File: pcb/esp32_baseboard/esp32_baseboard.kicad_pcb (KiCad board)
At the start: 2 copper layers, 190 x 100 mm, 50 parts, among them J1 Screw_12V_IN, J10 HOME HOME2, J12 HOME HOME3, J14 BUP-30S, J15 BUZZER 5V, J16 AOD4184 12V, J17 MSP3520 LCD, J18 EC11 ENC, J23 MSP3520 TP, J24 595_CTRL, J25 595_Q, J8 HOME HOME1, U1 ESP32-S3 DevKitC, U2 MP1584 5V, U3 TMC2209, U41 PC817, U42 PC817, U43 PC817, U44 PC817, U5 ULN2003 A1, U6 ULN2003 A2, U7 ULN2003 A3

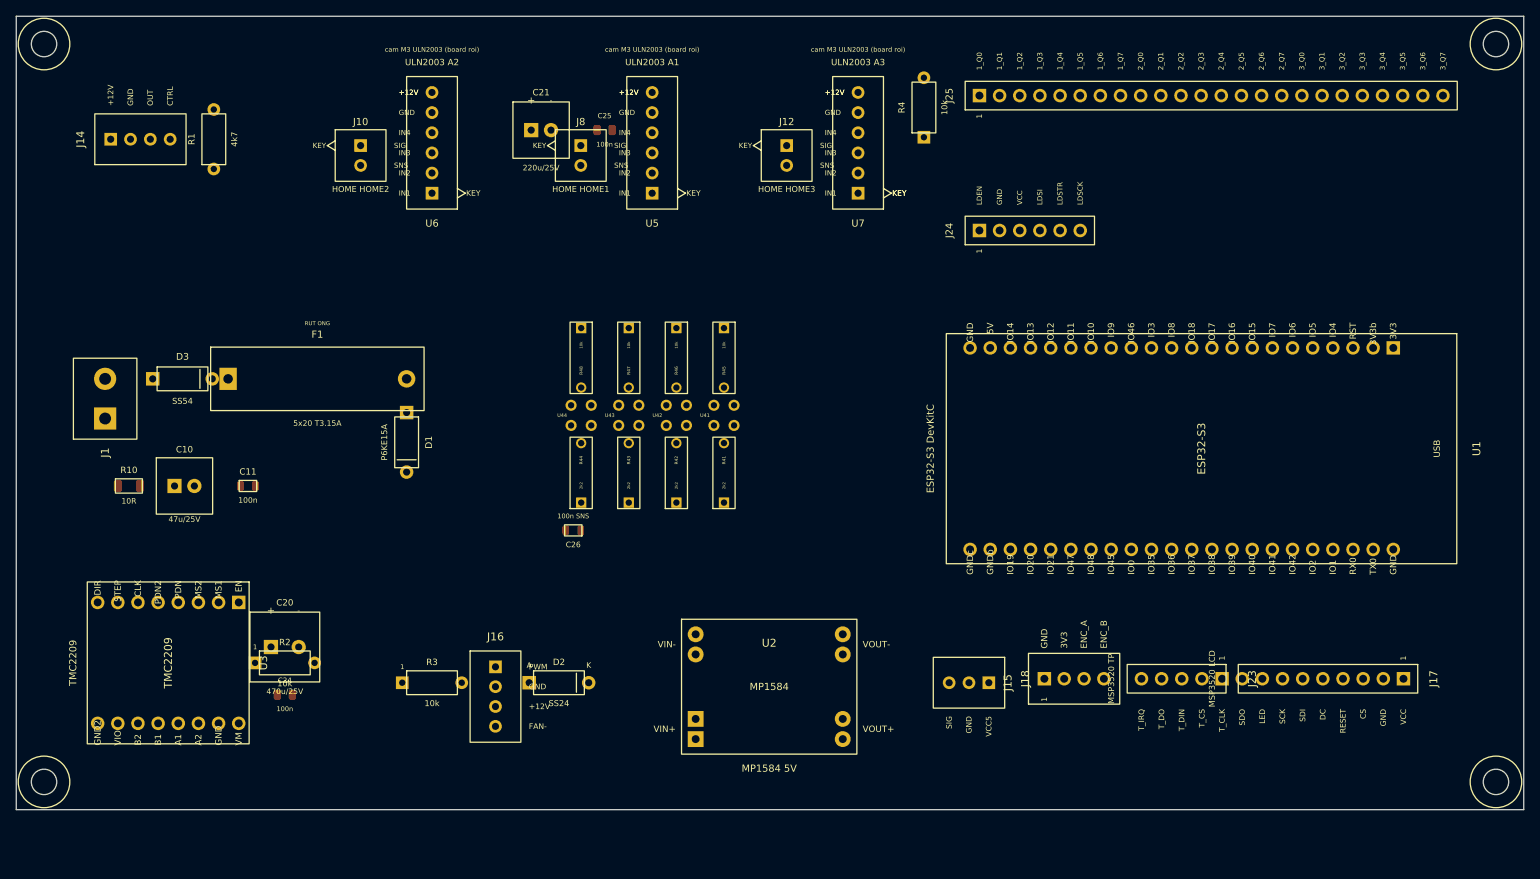
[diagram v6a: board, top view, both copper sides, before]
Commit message: update BOM và PCB với danh sách linh kiện mới loại bỏ màn hình cảm ứng và động cơ điều chỉnh độ rộng vách thay bằng led 7 thanh và bàn phím dán
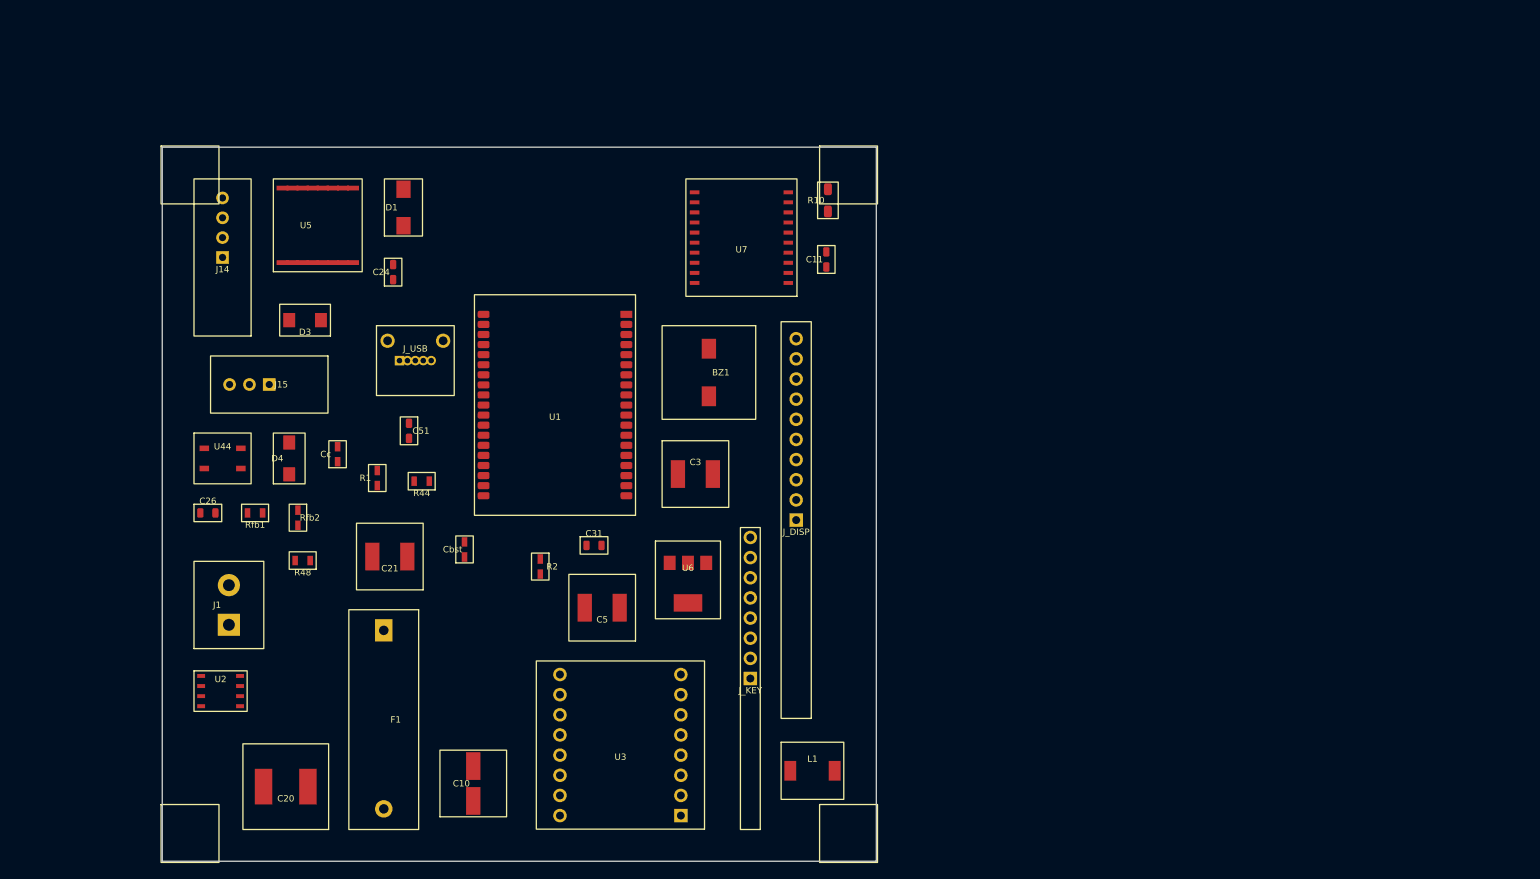
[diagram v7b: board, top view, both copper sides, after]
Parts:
- removed C25: 100n, ESP32_Carrier:C_0805_100n
- removed D2: SS24, ESP32_Carrier:Diode_TVS_DO41
- removed J10: HOME HOME2, ESP32_Carrier:JST_XH_02_Socket
- removed J12: HOME HOME3, ESP32_Carrier:JST_XH_02_Socket
- removed J16: AOD4184 12V, ESP32_Carrier:JST_XH_04_Socket
- removed J17: MSP3520 LCD, ESP32_Carrier:PinHeader_1x09_TFT_LCD
- removed J18: EC11 ENC, ESP32_Carrier:JST_XH_04_Socket
- removed J23: MSP3520 TP, ESP32_Carrier:PinHeader_1x05_TFT_TP
- removed J24: 595_CTRL, ESP32_Carrier:PinHeader_1x06_595CTRL
- removed J25: 595_Q, ESP32_Carrier:PinHeader_1x24_595Q
- removed J8: HOME HOME1, ESP32_Carrier:JST_XH_02_Socket
- removed R3, R4, R45, R46, R47: 10k, ESP32_Carrier:R_Axial_4k7_BUP
- removed R41, R42, R43: 2k2, ESP32_Carrier:R_Axial_4k7_BUP
- removed U41, U42, U43: PC817, ESP32_Carrier:PC817_DIP4
- added BZ1: BUZZ, ESP32_Carrier:Buzzer_SMD_5V, F.Cu at (118.9, 78.4)
- added C3: 47u/10V, ESP32_Carrier:CP_SMD_D6.3x5.8, F.Cu at (117.2, 91.2)
- added C31: 100n, ESP32_Carrier:C_0805_100n, F.Cu at (104.4, 100.2)
- added C5: 100u/16V, ESP32_Carrier:CP_SMD_D6.3x5.8, F.Cu at (105.4, 108.0)
- added C51: 100n, ESP32_Carrier:C_0805_100n, F.Cu at (81.1, 85.8)
- added Cbst: 10n, ESP32_Carrier:C_0805, F.Cu at (88.1, 100.7)
- added Cc: 3n3, ESP32_Carrier:C_0805, F.Cu at (72.1, 88.7)
- added D4: SS34, ESP32_Carrier:Diode_SMA, F.Cu at (66.0, 89.2)
- added J_DISP: 7SEG_EXT, ESP32_Carrier:PinHeader_1x10_7SEG, F.Cu at (129.9, 97.0)
- added J_KEY: KEYPAD_EXT, ESP32_Carrier:PinHeader_1x08_Keypad, F.Cu at (124.1, 117.0)
- added J_USB: USB, ESP32_Carrier:USB_MicroB, F.Cu at (81.9, 76.9)
- added L1: 10uH, ESP32_Carrier:L_SMD_6x6, F.Cu at (131.9, 128.6)
- added Rfb1: 52k3, ESP32_Carrier:R_0805_4k7, F.Cu at (61.7, 96.1)
- added Rfb2: 10k, ESP32_Carrier:R_0805_10k, F.Cu at (67.1, 96.7)
- C10: value 47u/25V -> 47u/50V; footprint ESP32_Carrier:CP_Radial_D6_47u_25V -> ESP32_Carrier:CP_SMD_D6.3x5.8
- C20: value 470u/25V -> 470u/50V; footprint ESP32_Carrier:CP_Radial_D8_470u_25V -> ESP32_Carrier:CP_SMD_D8x10
- C21: value 220u/25V -> 220u/50V; footprint ESP32_Carrier:CP_Radial_D6_100u_25V -> ESP32_Carrier:CP_SMD_D6.3x5.8
- C26: value 100n SNS -> 100n
- D1: value P6KE15A -> SMBJ26A; footprint ESP32_Carrier:Diode_TVS_DO41 -> ESP32_Carrier:Diode_SMB_TVS
- D3: footprint ESP32_Carrier:Diode_TVS_DO41 -> ESP32_Carrier:Diode_SMA
- F1: value 5x20 T3.15A -> T2.5A
- J1: value Screw_12V_IN -> 24V_IN
- J14: value BUP-30S -> BUP_U
- J15: value BUZZER 5V -> FIBER
- R1: footprint ESP32_Carrier:R_Axial_4k7_BUP -> ESP32_Carrier:R_0805_4k7
- R2, R48: footprint ESP32_Carrier:R_Axial_4k7_BUP -> ESP32_Carrier:R_0805_10k
- R44: footprint ESP32_Carrier:R_Axial_4k7_BUP -> ESP32_Carrier:R_0805_2k2
- U1: value ESP32-S3 DevKitC -> WROOM-32; footprint ESP32_Carrier:ESP32_S3_DevKitC_44Pin_Socket -> ESP32_Carrier:ESP32_WROOM_32
- U2: value MP1584 5V -> MP1584EN; footprint ESP32_Carrier:MP1584_5V3A -> ESP32_Carrier:MP1584EN_SOT23-8
- U3: value TMC2209 -> TMC_SOCK
- U44: footprint ESP32_Carrier:PC817_DIP4 -> ESP32_Carrier:PC817_SOP4
- U5: value ULN2003 A1 -> CH340C; footprint ESP32_Carrier:ULN2003_Module -> ESP32_Carrier:CH340C
- U6: value ULN2003 A2 -> AMS1117-3.3; footprint ESP32_Carrier:ULN2003_Module -> ESP32_Carrier:AMS1117_SOT223
- U7: value ULN2003 A3 -> TM1637; footprint ESP32_Carrier:ULN2003_Module -> ESP32_Carrier:TM1637_SOP20
- moved U1 105.9 mm to (99.5, 82.5), turned to 180 degrees
- moved J15 98.2 mm to (63.5, 79.9)
- moved R10 95.2 mm to (133.9, 56.7), turned to 90 degrees
- moved H2 83.3 mm to (136.5, 53.5)
- moved H4 81.9 mm to (136.5, 136.5)
- moved C11 78.3 mm to (133.7, 64.2), turned to 90 degrees
- moved U2 69.2 mm to (57.4, 118.6)
- moved U6 58.5 mm to (116.3, 104.5), turned to 0 degrees
- moved U3 57.9 mm to (107.7, 125.4), turned to 180 degrees
- moved C21 57.0 mm to (78.7, 101.6), turned to 180 degrees
- moved C24 55.0 mm to (79.1, 65.8), turned to 90 degrees
- moved C10 52.3 mm to (89.2, 130.2), turned to 90 degrees
- moved R1 47.4 mm to (77.1, 91.7)
- moved C26 46.1 mm to (55.8, 96.1), turned to 0 degrees
- moved U44 45.5 mm to (57.6, 89.2), turned to 0 degrees
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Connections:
- net +12V_PRE renamed +24V_PRE
- net +12V_RAW renamed +24V_RAW
- net MotA1 renamed /MotA1
- net MotA2 renamed /MotA2
- net MotB1 renamed /MotB1
- net MotB2 renamed /MotB2
- C10 pad 1: +12V_SNS -> +24V_SNS
- C11 pad 1: +12V_SNS -> +24V_SNS
- C20 pad 1: +12V -> +24V
- C21 pad 1: +12V -> +24V
- C24 pad 1: +12V -> +24V
- C26 pad 1: +12V_SNS -> +24V_SNS
- D1 pad 2: +12V -> +24V
- F1 pad 2: +12V -> +24V
- J14 pad 1: +12V_SNS -> +24V_SNS
- J14 pad 3: OPTO_IN4 -> /OPTO_IN_BUP
- J15 pad 1: +5V -> +24V_SNS
- J15 pad 3: BUZZER -> /OPTO_IN_BUP
- R1 pad 1: +12V_SNS -> +24V_SNS
- R1 pad 2: OPTO_IN4 -> /OPTO_IN_BUP
- R10 pad 1: +12V -> +24V
- R10 pad 2: +12V_SNS -> +24V_SNS
- R2 pad 1: EN_TMC -> +3V3
- R2 pad 2: +3V3 -> /EN_TMC
- R44 pad 1: OPTO_IN4 -> +24V_SNS
- R44 pad 2: OPTO_A4 -> /OPTO_IN_BUP
- R48 pad 2: OPTO_OUT4 -> /BUP
- U1 pad 1: +3V3 -> GND
- U1 pad 10: DIR -> /BUZZER
- U1 pad 11: EN_TMC -> /KEY_C0
- U1 pad 12: unconnected-(U1-IO8-Pad12) -> /KEY_R3
- U1 pad 13: BLOWER -> /KEY_R2
- U1 pad 14: TFT_RST -> /KEY_R1
- U1 pad 15: BUZZER -> GND
- U1 pad 16: SER -> /KEY_R0
- U1 pad 17: SRCLK -> unconnected-(U1-P17-Pad17)
- U1 pad 18: RCLK -> unconnected-(U1-P18-Pad18)
- U1 pad 19: OE_595 -> unconnected-(U1-P19-Pad19)
- U1 pad 20: unconnected-(U1-IO14-Pad20) -> GND
- U1 pad 21: +5V -> unconnected-(U1-P21-Pad21)
- U1 pad 22: GND -> unconnected-(U1-P22-Pad22)
- U1 pad 23: GND -> unconnected-(U1-P23-Pad23)
- U1 pad 26: OPTO_OUT1 -> /BUP
- U1 pad 27: OPTO_OUT2 -> /STEP
- U1 pad 28: TFT_CS -> /DIR
- U1 pad 29: ENC_B -> /KEY_C3
- U1 pad 3: unconnected-(U1-RST-Pad3) -> +3V3
- U1 pad 30: TFT_MOSI -> /EN_TMC
- U1 pad 31: TFT_SCK -> unconnected-(U1-P31-Pad31)
- U1 pad 32: ENC_A -> unconnected-(U1-P32-Pad32)
- U1 pad 34: unconnected-(U1-IO36-Pad34) -> /UART_RX
- U1 pad 35: unconnected-(U1-IO35-Pad35) -> /UART_TX
- U1 pad 36: unconnected-(U1-IO0-Pad36) -> /TM_CLK
- U1 pad 37: TFT_BL -> /TM_DIO
- U1 pad 38: T_CS -> GND
- U1 pad 4: OPTO_OUT3 -> unconnected-(U1-P4-Pad4)
- U1 pad 5: OPTO_OUT4 -> unconnected-(U1-P5-Pad5)
- U1 pad 6: T_IRQ -> unconnected-(U1-P6-Pad6)
- U1 pad 8: unconnected-(U1-IO15-Pad8) -> /KEY_C2
- U1 pad 9: STEP -> /KEY_C1
- U2 pad 1: +12V -> /BUCK_SW
- U2 pad 2: GND -> +24V
- U2 pad 3: GND -> /BUCK_COMP
- U2 pad 4: +5V -> /BUCK_FB
- U3 pad 1: EN_TMC -> /EN_TMC
- U3 pad 7: STEP -> /STEP
- U3 pad 8: DIR -> /DIR
- U3 pad 9: +12V -> +24V
- U44 pad 1: OPTO_A4 -> /OPTO_IN_BUP
- U44 pad 4: OPTO_OUT4 -> /BUP
- U5 pad 1: SR_Q0 -> GND
- U5 pad 2: SR_Q1 -> /UART_RX
- U5 pad 3: SR_Q2 -> /UART_TX
- U5 pad 4: SR_Q3 -> +3V3
- U5 pad 5: GND -> /USB_DP
- U5 pad 6: +12V -> /USB_DM
- U6 pad 1: SR_Q4 -> GND
- U6 pad 2: SR_Q5 -> +3V3
- U6 pad 3: SR_Q6 -> +5V
- U7 pad 1: SR_Q8 -> /TM_G1
- U7 pad 2: SR_Q9 -> /TM_G2
- U7 pad 3: SR_Q10 -> /TM_G3
- U7 pad 4: SR_Q11 -> unconnected-(U7-P4-Pad4)
- U7 pad 5: GND -> unconnected-(U7-P5-Pad5)
- U7 pad 6: +12V -> unconnected-(U7-P6-Pad6)
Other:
- board size 190 x 100 mm -> 90 x 90 mm
- board text added: "90x90 placement-only — ANT keepout north of U1; J1 west"
- board text added: "ANT KEEPOUT"
- board text added: "J_DISP=7SEG ext | J_KEY=keypad ext | J14/J15 fit ONE"

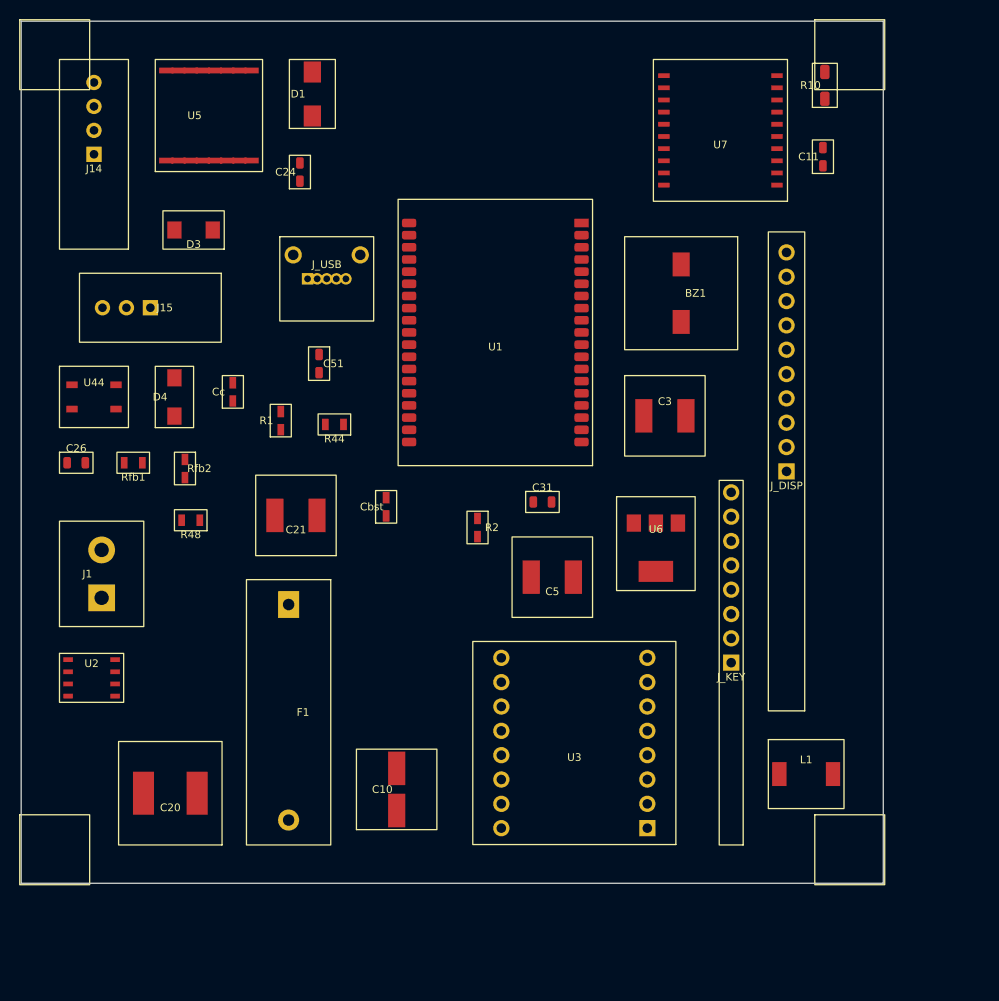
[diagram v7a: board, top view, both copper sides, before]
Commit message: thêm usb để nạp chương trình và loại bỏ buzz
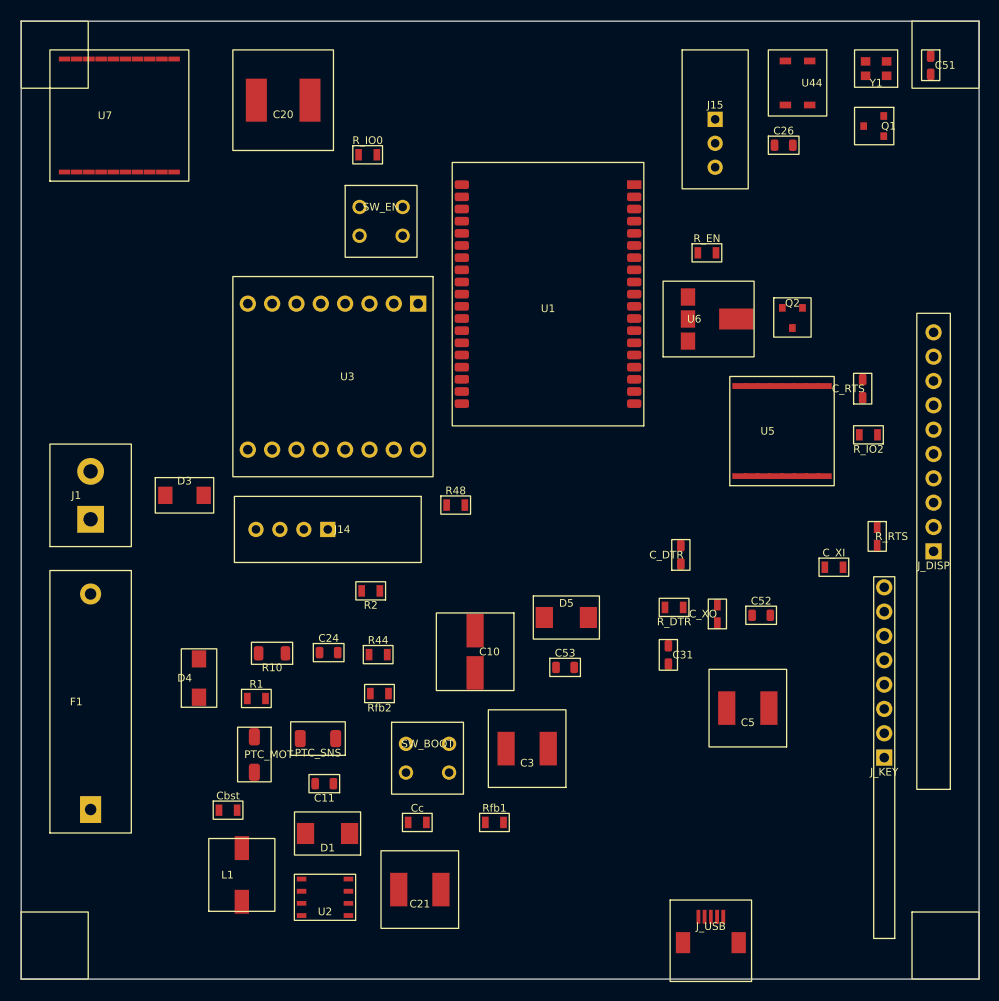
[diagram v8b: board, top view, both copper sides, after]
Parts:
- removed BZ1: BUZZ, ESP32_Carrier:Buzzer_SMD_5V
- added C52: 100n, ESP32_Carrier:C_0805_100n, F.Cu at (127.3, 112.0)
- added C53: 100n, ESP32_Carrier:C_0805_100n, F.Cu at (106.8, 117.5)
- added C_DTR: 100n, ESP32_Carrier:C_0805_100n, F.Cu at (118.9, 105.7)
- added C_RTS: 100n, ESP32_Carrier:C_0805_100n, F.Cu at (137.9, 88.4)
- added C_XI: 22p, ESP32_Carrier:C_0805, F.Cu at (134.8, 107.0)
- added C_XO: 22p, ESP32_Carrier:C_0805, F.Cu at (122.7, 111.9)
- added D5: SMBJ5.0A, ESP32_Carrier:Diode_SMB_TVS, F.Cu at (106.9, 112.3)
- added PTC_MOT: 1.1A, ESP32_Carrier:PTC_1812, F.Cu at (74.3, 126.6)
- added PTC_SNS: 0.2A, ESP32_Carrier:PTC_1812, F.Cu at (81.0, 124.9)
- added Q1: S8050, ESP32_Carrier:S8050_SOT23, F.Cu at (139.1, 61.0)
- added Q2: S8050, ESP32_Carrier:S8050_SOT23, F.Cu at (130.5, 80.9)
- added R_DTR: 10k, ESP32_Carrier:R_0805_10k, F.Cu at (118.2, 111.2)
- added R_EN: 10k, ESP32_Carrier:R_0805_10k, F.Cu at (121.6, 74.2)
- added R_IO0: 10k, ESP32_Carrier:R_0805_10k, F.Cu at (86.2, 64.0)
- added R_IO2: 10k, ESP32_Carrier:R_0805_10k, F.Cu at (138.5, 93.2)
- added R_RTS: 10k, ESP32_Carrier:R_0805_10k, F.Cu at (139.4, 103.8)
- added SW_BOOT: BOOT, ESP32_Carrier:SW_Push_6mm, F.Cu at (92.4, 126.9)
- added SW_EN: EN, ESP32_Carrier:SW_Push_6mm, F.Cu at (87.6, 70.9)
- added Y1: 12MHz, ESP32_Carrier:Crystal_SMD_3225, F.Cu at (139.2, 55.0)
- F1: value T2.5A -> T2A
- J_USB: value USB -> USB_MicroB
- R10: value 10R -> 22R; footprint ESP32_Carrier:R_1206_10R -> ESP32_Carrier:R_1206_22R
- moved C11 83.6 mm to (81.6, 129.6), turned to 180 degrees
- moved R10 82.7 mm to (76.2, 116.0), turned to 180 degrees
- moved C26 80.9 mm to (129.6, 63.0)
- moved U44 80.4 mm to (131.1, 56.5), turned to 270 degrees
- moved J_USB 79.9 mm to (122.0, 146.0)
- moved D1 77.2 mm to (82.0, 134.8), turned to 180 degrees
- moved C20 73.3 mm to (77.3, 58.2)
- moved C51 71.0 mm to (144.9, 54.6)
- moved U5 68.3 mm to (129.4, 92.8)
- moved U7 62.8 mm to (60.2, 59.9), turned to 90 degrees
- moved J15 62.2 mm to (122.5, 60.2), turned to 0 degrees
- moved L1 59.8 mm to (73.0, 139.1), turned to 90 degrees
- moved Rfb1 53.2 mm to (99.4, 133.7), turned to 0 degrees
- moved C24 50.3 mm to (82.1, 115.9), turned to 0 degrees
- moved Cc 48.9 mm to (91.4, 133.7), turned to 0 degrees
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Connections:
- C20 pad 1: +24V -> +24V_MOT
- C24 pad 1: +24V -> +24V_MOT
- J14 pad 4: unconnected-(J14-ENC_B-Pad4) -> (no net)
- J_USB pad 4: unconnected-(J_USB-P4-Pad4) -> (no net)
- R10 pad 1: +24V -> +24V_SNS_PRE
- U1 pad 10: /BUZZER -> (no net)
- U1 pad 17: unconnected-(U1-P17-Pad17) -> (no net)
- U1 pad 18: unconnected-(U1-P18-Pad18) -> (no net)
- U1 pad 19: unconnected-(U1-P19-Pad19) -> (no net)
- U1 pad 21: unconnected-(U1-P21-Pad21) -> (no net)
- U1 pad 22: unconnected-(U1-P22-Pad22) -> (no net)
- U1 pad 23: unconnected-(U1-P23-Pad23) -> (no net)
- U1 pad 24: unconnected-(U1-P24-Pad24) -> /IO2
- U1 pad 25: unconnected-(U1-P25-Pad25) -> /IO0
- U1 pad 3: +3V3 -> /EN
- U1 pad 31: unconnected-(U1-P31-Pad31) -> (no net)
- U1 pad 32: unconnected-(U1-P32-Pad32) -> (no net)
- U1 pad 33: unconnected-(U1-P33-Pad33) -> (no net)
- U1 pad 4: unconnected-(U1-P4-Pad4) -> (no net)
- U1 pad 5: unconnected-(U1-P5-Pad5) -> (no net)
- U1 pad 6: unconnected-(U1-P6-Pad6) -> (no net)
- U1 pad 7: unconnected-(U1-P7-Pad7) -> (no net)
- U2 pad 7: unconnected-(U2-P7-Pad7) -> (no net)
- U3 pad 2: unconnected-(U3-MS1-Pad2) -> (no net)
- U3 pad 3: unconnected-(U3-MS2-Pad3) -> (no net)
- U3 pad 4: unconnected-(U3-PDN-Pad4) -> (no net)
- U3 pad 5: unconnected-(U3-PDN2-Pad5) -> (no net)
- U3 pad 6: unconnected-(U3-CLK-Pad6) -> (no net)
- U3 pad 9: +24V -> +24V_MOT
- U5 pad 10: unconnected-(U5-P10-Pad10) -> /DTR
- U5 pad 11: unconnected-(U5-P11-Pad11) -> (no net)
- U5 pad 12: unconnected-(U5-P12-Pad12) -> (no net)
- U5 pad 13: unconnected-(U5-P13-Pad13) -> (no net)
- U5 pad 14: unconnected-(U5-P14-Pad14) -> (no net)
- U5 pad 15: unconnected-(U5-P15-Pad15) -> /RTS
- U5 pad 7: unconnected-(U5-P7-Pad7) -> /CH340_XI
- U5 pad 8: unconnected-(U5-P8-Pad8) -> /CH340_XO
- U5 pad 9: unconnected-(U5-P9-Pad9) -> (no net)
- U7 pad 14: unconnected-(U7-P14-Pad14) -> (no net)
- U7 pad 19: unconnected-(U7-P19-Pad19) -> (no net)
- U7 pad 20: unconnected-(U7-P20-Pad20) -> (no net)
- U7 pad 4: unconnected-(U7-P4-Pad4) -> (no net)
- U7 pad 5: unconnected-(U7-P5-Pad5) -> (no net)
- U7 pad 6: unconnected-(U7-P6-Pad6) -> (no net)
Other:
- board size 90 x 90 mm -> 100 x 100 mm
- board text added: "100x100 placement-only — ANT keepout north of U1; J1 west"
- board text removed: "90x90 placement-only — ANT keepout north of U1; J1 west"
